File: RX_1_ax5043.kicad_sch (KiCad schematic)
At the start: 21 parts, among them J6 2118714-2, P5 CONUFL001-SMD-T, Q3 DMP2037U, U21 AX5043

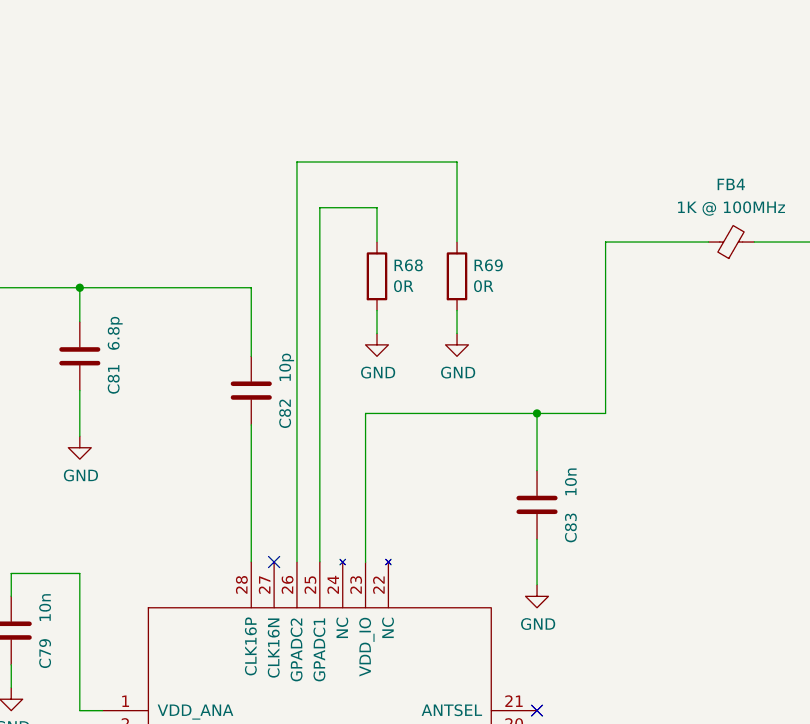
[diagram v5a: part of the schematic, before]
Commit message: More 0402 updates and cleanups
Signed-off-by: Corey Minyard <corey@minyard.net>
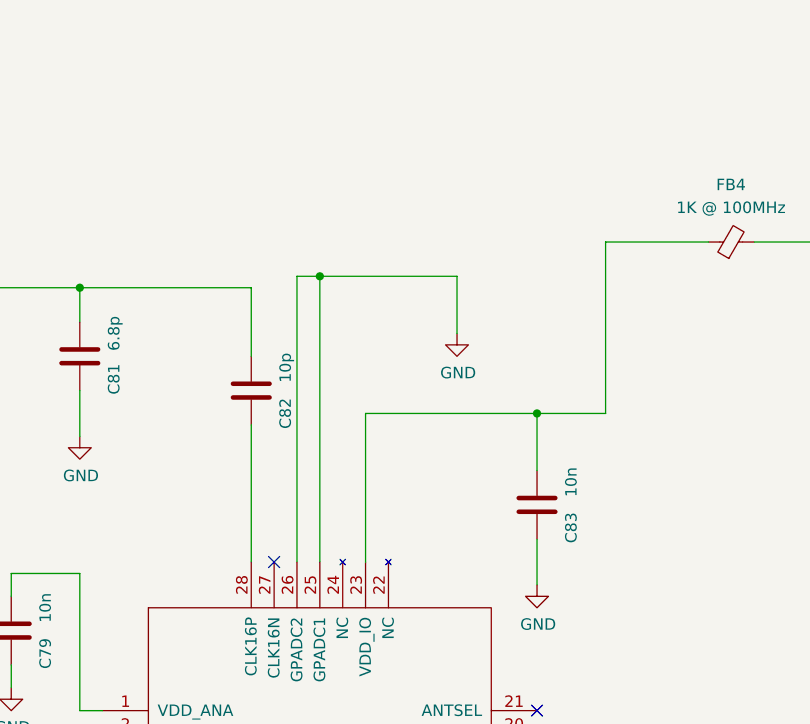
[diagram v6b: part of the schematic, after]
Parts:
- removed R68, R69: 0R, Resistor_SMD:R_0603_1608Metric_Pad0.98x0.95mm_HandSolder, symbol Device:R
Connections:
- net GND: now also U21.25 (GPADC1), U21.26 (GPADC2)
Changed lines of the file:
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@@
 	)
 	(junction
+		(at 220.98 80.01)
+		(diameter 0)
+		(color 0 0 0 0)
+	)
+	(junction
 		(at 119.38 62.23)
 		(diameter 0)
@@
 	(wire
 		(pts
-			(xy 220.98 72.39) (xy 227.33 72.39)
-		)
-		(stroke
-			(width 0)
-			(type default)
-		)
-	)
-	(wire
-		(pts
 			(xy 194.31 113.03) (xy 186.69 113.03)
 		)
@@
 	(wire
 		(pts
-			(xy 236.22 67.31) (xy 236.22 76.2)
+			(xy 173.99 129.54) (xy 176.53 129.54)
 		)
 		(stroke
@@
 	(wire
 		(pts
-			(xy 173.99 129.54) (xy 176.53 129.54)
+			(xy 135.89 129.54) (xy 139.7 129.54)
 		)
 		(stroke
@@
 	(wire
 		(pts
-			(xy 135.89 129.54) (xy 139.7 129.54)
+			(xy 218.44 80.01) (xy 218.44 111.76)
 		)
 		(stroke
@@
 	(wire
 		(pts
+			(xy 218.44 80.01) (xy 220.98 80.01)
+		)
+		(stroke
+			(width 0)
+			(type default)
+		)
+	)
+	(wire
+		(pts
 			(xy 119.38 46.99) (xy 124.46 46.99)
 		)
@@
 	(wire
 		(pts
-			(xy 220.98 72.39) (xy 220.98 111.76)
+			(xy 236.22 80.01) (xy 220.98 80.01)
 		)
 		(stroke
@@
 	(wire
 		(pts
-			(xy 119.38 52.07) (xy 119.38 54.61)
+			(xy 220.98 80.01) (xy 220.98 111.76)
 		)
 		(stroke
@@
 	(wire
 		(pts
-			(xy 176.53 133.35) (xy 176.53 129.54)
+			(xy 119.38 52.07) (xy 119.38 54.61)
 		)
 		(stroke
@@
 	(wire
 		(pts
-			(xy 204.47 165.1) (xy 204.47 172.72)
+			(xy 176.53 133.35) (xy 176.53 129.54)
 		)
 		(stroke
@@
 	(wire
 		(pts
-			(xy 196.85 130.81) (xy 193.04 130.81)
+			(xy 204.47 165.1) (xy 204.47 172.72)
 		)
 		(stroke
@@
 	(wire
 		(pts
-			(xy 119.38 46.99) (xy 119.38 49.53)
+			(xy 196.85 130.81) (xy 193.04 130.81)
 		)
 		(stroke
@@
 	(wire
 		(pts
-			(xy 231.14 157.48) (xy 231.14 161.29)
+			(xy 119.38 46.99) (xy 119.38 49.53)
 		)
 		(stroke
@@
 	(wire
 		(pts
-			(xy 226.06 95.25) (xy 245.11 95.25)
+			(xy 231.14 157.48) (xy 231.14 161.29)
 		)
 		(stroke
@@
 	(wire
 		(pts
-			(xy 173.99 129.54) (xy 173.99 142.24)
+			(xy 226.06 95.25) (xy 245.11 95.25)
 		)
 		(stroke
@@
 	(wire
 		(pts
-			(xy 236.22 83.82) (xy 236.22 86.36)
+			(xy 173.99 129.54) (xy 173.99 142.24)
 		)
 		(stroke
@@
 	(wire
 		(pts
-			(xy 227.33 83.82) (xy 227.33 86.36)
-		)
-		(stroke
-			(width 0)
-			(type default)
-		)
-	)
-	(wire
-		(pts
 			(xy 124.46 138.43) (xy 124.46 139.7)
 		)
@@
 	(wire
 		(pts
-			(xy 218.44 67.31) (xy 236.22 67.31)
-		)
-		(stroke
-			(width 0)
-			(type default)
-		)
-	)
-	(wire
-		(pts
 			(xy 119.38 57.15) (xy 119.38 59.69)
 		)
@@
 	(wire
 		(pts
-			(xy 252.73 76.2) (xy 252.73 95.25)
+			(xy 236.22 80.01) (xy 236.22 86.36)
 		)
 		(stroke
@@
 	(wire
 		(pts
-			(xy 119.38 64.77) (xy 119.38 69.85)
+			(xy 252.73 76.2) (xy 252.73 95.25)
 		)
 		(stroke
@@
 	(wire
 		(pts
-			(xy 245.11 143.51) (xy 251.46 143.51)
+			(xy 119.38 64.77) (xy 119.38 69.85)
 		)
 		(stroke
@@
 	(wire
 		(pts
-			(xy 259.08 143.51) (xy 269.24 143.51)
+			(xy 245.11 143.51) (xy 251.46 143.51)
 		)
 		(stroke
@@
 	(wire
 		(pts
-			(xy 245.11 140.97) (xy 269.24 140.97)
+			(xy 259.08 143.51) (xy 269.24 143.51)
 		)
 		(stroke
@@
 	(wire
 		(pts
-			(xy 119.38 54.61) (xy 124.46 54.61)
+			(xy 245.11 140.97) (xy 269.24 140.97)
 		)
 		(stroke
@@
 	(wire
 		(pts
-			(xy 194.31 92.71) (xy 194.31 97.79)
+			(xy 119.38 54.61) (xy 124.46 54.61)
 		)
 		(stroke
@@
 	(wire
 		(pts
-			(xy 140.97 139.7) (xy 135.89 139.7)
+			(xy 194.31 92.71) (xy 194.31 97.79)
 		)
 		(stroke
@@
 	(wire
 		(pts
-			(xy 218.44 67.31) (xy 218.44 111.76)
+			(xy 140.97 139.7) (xy 135.89 139.7)
 		)
 		(stroke
@@
 	(wire
 		(pts
-			(xy 227.33 72.39) (xy 227.33 76.2)
-		)
-		(stroke
-			(width 0)
-			(type default)
-		)
-	)
-	(wire
-		(pts
 			(xy 269.24 76.2) (xy 279.4 76.2)
 		)
@@
 	)
 	(symbol
-		(lib_id "power:GND")
-		(at 227.33 86.36 0)
-		(unit 1)
-		(exclude_from_sim no)
-		(in_bom yes)
-		(on_board yes)
-		(dnp no)
-		(property "Reference" "#PWR0177"
-			(at 227.33 92.71 0)
-			(effects
-				(font
-					(size 1.27 1.27)
-				)
-				(hide yes)
-			)
-		)
-		(property "Value" "GND"
-			(at 227.457 90.7542 0)
-			(effects
-				(font
-					(size 1.27 1.27)
-				)
-			)
-		)
-		(property "Footprint" ""
-			(at 227.33 86.36 0)
-			(effects
-				(font
-					(size 1.27 1.27)
-				)
-				(hide yes)
-			)
-		)
-		(property "Datasheet" ""
-			(at 227.33 86.36 0)
-			(effects
-				(font
-					(size 1.27 1.27)
-				)
-				(hide yes)
-			)
-		)
-		(property "Description" ""
-			(at 227.33 86.36 0)
-			(effects
-				(font
-					(size 1.27 1.27)
-				)
-			)
-		)
-		(pin "1"
-		)
-		(instances
-			(project "PacSat_Dev_RevD_240614"
-				(path "/cc9f42d2-6985-41ac-acab-5ab7b01c5b38/d9a83ee4-3280-49b9-88b8-54d26cbd8ed1/bc27fde3-8cca-4897-854d-674b6eeb65de"
-					(reference "#PWR0177")
-					(unit 1)
-				)
-			)
-		)
-	)
-	(symbol
 		(lib_id "PACSAT_DEV_misc:U_FL")
 		(at 123.19 129.54 0)
@@
 	)
 	(symbol
-		(lib_id "Device:R")
-		(at 236.22 80.01 0)
-		(unit 1)
-		(exclude_from_sim no)
-		(in_bom yes)
-		(on_board yes)
-		(dnp no)
-		(property "Reference" "R69"
-			(at 237.998 78.8416 0)
-			(effects
-				(font
-					(size 1.27 1.27)
-				)
-				(justify left)
-			)
-		)
-		(property "Value" "0R"
-			(at 237.998 81.153 0)
-			(effects
-				(font
-					(size 1.27 1.27)
-				)
-				(justify left)
-			)
-		)
-		(property "Footprint" "Resistor_SMD:R_0603_1608Metric_Pad0.98x0.95mm_HandSolder"
-			(at 234.442 80.01 90)
-			(effects
-				(font
-					(size 1.27 1.27)
-				)
-				(hide yes)
-			)
-		)
-		(property "Datasheet" "~"
-			(at 236.22 80.01 0)
-			(effects
-				(font
-					(size 1.27 1.27)
-				)
-			)
-		)
-		(property "Description" ""
-			(at 236.22 80.01 0)
-			(effects
-				(font
-					(size 1.27 1.27)
-				)
-			)
-		)
-		(pin "1"
-		)
-		(pin "2"
-		)
-		(instances
-			(project "PacSat_Dev_RevD_240614"
-				(path "/cc9f42d2-6985-41ac-acab-5ab7b01c5b38/d9a83ee4-3280-49b9-88b8-54d26cbd8ed1/bc27fde3-8cca-4897-854d-674b6eeb65de"
-					(reference "R69")
-					(unit 1)
-				)
-			)
-		)
-	)
-	(symbol
 		(lib_id "Device:C")
 		(at 153.67 146.05 180)
@@
 					(unit 1)
 				)
-			)
-		)
-	)
-	(symbol
-		(lib_id "Device:R")
-		(at 227.33 80.01 0)
-		(unit 1)
-		(exclude_from_sim no)
-		(in_bom yes)
-		(on_board yes)
-		(dnp no)
-		(property "Reference" "R68"
-			(at 229.108 78.8416 0)
-			(effects
-				(font
-					(size 1.27 1.27)
-				)
-				(justify left)
-			)
-		)
-		(property "Value" "0R"
-			(at 229.108 81.153 0)
-			(effects
-				(font
-					(size 1.27 1.27)
-				)
-				(justify left)
-			)
-		)
-		(property "Footprint" "Resistor_SMD:R_0603_1608Metric_Pad0.98x0.95mm_HandSolder"
-			(at 225.552 80.01 90)
-			(effects
-				(font
-					(size 1.27 1.27)
-				)
-				(hide yes)
-			)
-		)
-		(property "Datasheet" "~"
-			(at 227.33 80.01 0)
-			(effects
-				(font
-					(size 1.27 1.27)
-				)
-			)
-		)
-		(property "Description" ""
-			(at 227.33 80.01 0)
-			(effects
-				(font
-					(size 1.27 1.27)
-				)
-			)
-		)
-		(pin "1"
-		)
-		(pin "2"
-		)
-		(instances
-			(project "PacSat_Dev_RevD_240614"
-				(path "/cc9f42d2-6985-41ac-acab-5ab7b01c5b38/d9a83ee4-3280-49b9-88b8-54d26cbd8ed1/bc27fde3-8cca-4897-854d-674b6eeb65de"
-					(reference "R68")
-					(unit 1)
-				)

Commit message: Change appropriate passives to 0402 on the receive AX5043s
Signed-off-by: Corey Minyard <corey@minyard.net>
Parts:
- C76: footprint Resistor_SMD:R_0603_1608Metric_Pad0.98x0.95mm_HandSolder -> Capacitor_SMD:C_0402_1005Metric_Pad0.74x0.62mm_HandSolder
- C77, C78, C80, C81, C82, C83: footprint Capacitor_SMD:C_0603_1608Metric_Pad1.08x0.95mm_HandSolder -> Capacitor_SMD:C_0402_1005Metric_Pad0.74x0.62mm_HandSolder
- R67, R70: footprint Resistor_SMD:R_0603_1608Metric_Pad0.98x0.95mm_HandSolder -> Resistor_SMD:R_0402_1005Metric_Pad0.72x0.64mm_HandSolder
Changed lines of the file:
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@@
 			)
 		)
-		(property "Footprint" "Resistor_SMD:R_0603_1608Metric_Pad0.98x0.95mm_HandSolder"
+		(property "Footprint" "Resistor_SMD:R_0402_1005Metric_Pad0.72x0.64mm_HandSolder"
 			(at 255.27 145.288 90)
 			(effects
@@
 			)
 		)
-		(property "Footprint" "Capacitor_SMD:C_0603_1608Metric_Pad1.08x0.95mm_HandSolder"
+		(property "Footprint" "Capacitor_SMD:C_0402_1005Metric_Pad0.74x0.62mm_HandSolder"
 			(at 189.5348 149.86 0)
 			(effects
@@
 			)
 		)
-		(property "Footprint" "Capacitor_SMD:C_0603_1608Metric_Pad1.08x0.95mm_HandSolder"
+		(property "Footprint" "Capacitor_SMD:C_0402_1005Metric_Pad0.74x0.62mm_HandSolder"
 			(at 214.3252 96.52 0)
 			(effects
@@
 			)
 		)
-		(property "Footprint" "Capacitor_SMD:C_0603_1608Metric_Pad1.08x0.95mm_HandSolder"
+		(property "Footprint" "Capacitor_SMD:C_0402_1005Metric_Pad0.74x0.62mm_HandSolder"
 			(at 195.2752 92.71 0)
 			(effects
@@
 			)
 		)
-		(property "Footprint" "Capacitor_SMD:C_0603_1608Metric_Pad1.08x0.95mm_HandSolder"
+		(property "Footprint" "Capacitor_SMD:C_0402_1005Metric_Pad0.74x0.62mm_HandSolder"
 			(at 246.0752 109.22 0)
 			(effects
@@
 			)
 		)
-		(property "Footprint" "Resistor_SMD:R_0603_1608Metric_Pad0.98x0.95mm_HandSolder"
+		(property "Footprint" "Capacitor_SMD:C_0402_1005Metric_Pad0.74x0.62mm_HandSolder"
 			(at 134.3152 124.46 0)
 			(effects
@@
 			)
 		)
-		(property "Footprint" "Capacitor_SMD:C_0603_1608Metric_Pad1.08x0.95mm_HandSolder"
+		(property "Footprint" "Capacitor_SMD:C_0402_1005Metric_Pad0.74x0.62mm_HandSolder"
 			(at 140.97 140.6652 0)
 			(effects
@@
 			)
 		)
-		(property "Footprint" "Capacitor_SMD:C_0603_1608Metric_Pad1.08x0.95mm_HandSolder"
+		(property "Footprint" "Capacitor_SMD:C_0402_1005Metric_Pad0.74x0.62mm_HandSolder"
 			(at 152.7048 142.24 0)
 			(effects
@@
 			)
 		)
-		(property "Footprint" "Resistor_SMD:R_0603_1608Metric_Pad0.98x0.95mm_HandSolder"
+		(property "Footprint" "Resistor_SMD:R_0402_1005Metric_Pad0.72x0.64mm_HandSolder"
 			(at 177.292 149.86 90)
 			(effects

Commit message: Work on cleaning up all values for things
Signed-off-by: Corey Minyard <corey@minyard.net>
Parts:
- C77, C78: value 15p -> 15p 1%
- L17: value 1n Q=12 -> 1n Q=77; footprint Inductor_SMD:L_0603_1608Metric_Pad1.05x0.95mm_HandSolder -> Inductor_SMD:L_0402_1005Metric_Pad0.77x0.64mm_HandSolder
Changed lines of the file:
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@@
 			)
 		)
-		(property "Value" "1n Q=12"
+		(property "Value" "1n Q=77"
 			(at 175.514 145.796 90)
 			(effects
@@
 			)
 		)
-		(property "Footprint" "Inductor_SMD:L_0603_1608Metric_Pad1.05x0.95mm_HandSolder"
+		(property "Footprint" "Inductor_SMD:L_0402_1005Metric_Pad0.77x0.64mm_HandSolder"
 			(at 173.99 146.05 0)
 			(effects
@@
 		)
 		(property "Value" "78n 2% Q=28"
-			(at 165.608 146.05 90)
+			(at 165.862 147.066 90)
 			(effects
 				(font
@@
 			)
 		)
-		(property "Value" "15p"
+		(property "Value" "15p 1%"
 			(at 148.59 137.16 90)
 			(effects
@@
 			)
 		)
-		(property "Value" "15p"
+		(property "Value" "15p 1%"
 			(at 156.21 149.86 90)
 			(effects
